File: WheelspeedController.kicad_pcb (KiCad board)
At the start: 2 copper layers, 63.5 x 35.3 mm, 70 parts, among them J1 DEUTSCH DT Inp, J2 DEUTSCH DT Data, J3 DEUTSCH DT Out, J4 Conn_01x02, J6 SWD, SW1 SW_SPDT, SW2 SW_SPDT, U1 LMR51420, U2 AMS1117-3.3, U3 STM32F105RCTx, U4 SN65HVD230, Y1 16MHz

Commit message: fixed borders
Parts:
- moved TP2 2.17 mm to (118.4, 102.4)
- moved TP4 2.05 mm to (61.0, 102.4)
- moved TP3 0.57 mm to (118.4, 73.2)
- moved TP1 0.25 mm to (61.0, 73.2)
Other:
- board size 63.5 x 35.3 mm -> 63.5 x 35.6 mm
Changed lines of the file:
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@@
   )
   (footprint "TestPoint:TestPoint_Plated_Hole_D3.0mm" (layer "F.Cu")
-    (at 61.976 100.584)
+    (at 60.96 102.362)
     (descr "Plated Hole as test Point, diameter 3.0mm")
     (tags "test point plated hole")
@@
   )
   (footprint "TestPoint:TestPoint_Plated_Hole_D3.0mm" (layer "F.Cu")
-    (at 60.96 73.406)
+    (at 60.96 73.152)
     (descr "Plated Hole as test Point, diameter 3.0mm")
     (tags "test point plated hole")
@@
   )
   (footprint "TestPoint:TestPoint_Plated_Hole_D3.0mm" (layer "F.Cu")
-    (at 116.332 101.6)
+    (at 118.364 102.362)
     (descr "Plated Hole as test Point, diameter 3.0mm")
     (tags "test point plated hole")
@@
   )
   (footprint "TestPoint:TestPoint_Plated_Hole_D3.0mm" (layer "F.Cu")
-    (at 117.856 73.406)
+    (at 118.364 73.152)
     (descr "Plated Hole as test Point, diameter 3.0mm")
     (tags "test point plated hole")
@@
     )
   )
-  (gr_rect (start 57.917 70.133) (end 121.417 105.439) (layer "Edge.Cuts") (width 0.1) (fill none))
+  (gr_rect (start 57.917 69.879) (end 121.417 105.439) (layer "Edge.Cuts") (width 0.1) (fill none))
   (segment (start 99.581 87.127) (end 100.579 87.127) (width 0.25) (layer "F.Cu") (net 1))
   (segment (start 90.113 91.243) (end 90.932 90.424) (width 0.25) (layer "F.Cu") (net 1))

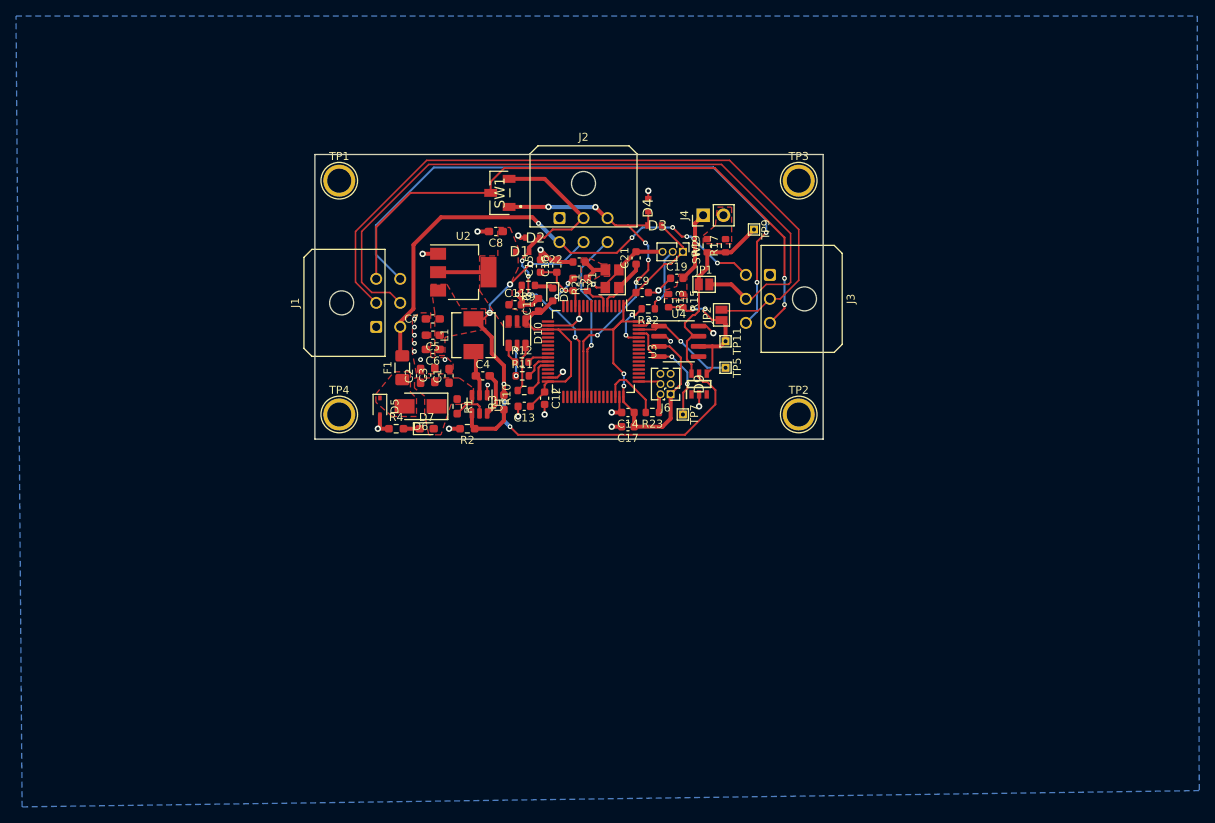
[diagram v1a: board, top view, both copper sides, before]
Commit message: Updated to 4 layers. Bit late
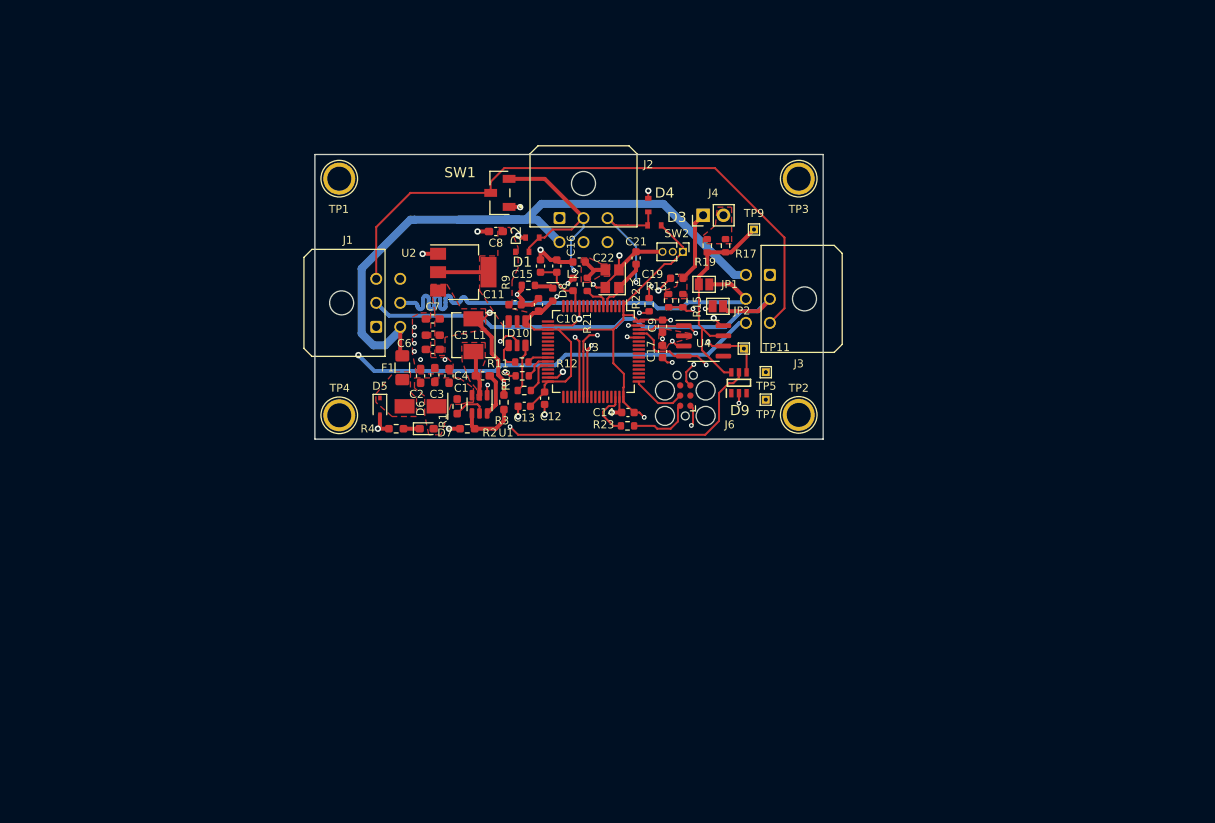
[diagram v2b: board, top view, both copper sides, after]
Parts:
- J6: footprint Connector_PinHeader_1.27mm:PinHeader_2x03_P1.27mm_Vertical -> Connector:Tag-Connect_TC2030-IDC-FP_2x03_P1.27mm_Vertical
- moved TP7 10.5 mm to (114.2, 100.5)
- moved C17 10.3 mm to (101.3, 94.5), turned to 90 degrees
- moved TP5 5.06 mm to (114.2, 97.1)
- moved D9 4.98 mm to (110.9, 98.4)
- moved C9 4.92 mm to (101.3, 91.3), turned to -90 degrees
- moved R23 3.52 mm to (97.0, 103.8)
- moved U4 3.10 mm to (106.5, 93.2)
- moved TP11 2.46 mm to (111.5, 94.1)
- moved J6 1.84 mm to (104.2, 100.0), turned to 90 degrees
- moved JP2 1.16 mm to (108.3, 88.8), turned to 0 degrees
- moved R22 0.52 mm to (99.7, 88.6), turned to -90 degrees
- moved TP1 0.25 mm to (61.0, 72.9)
- moved TP3 0.25 mm to (118.4, 72.9)
- moved TP4 0.10 mm to (61.0, 102.5)
- moved TP2 0.05 mm to (118.4, 102.4)
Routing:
- net /CAN+: track 90.7 -> 57.9 mm
- net /CAN-: track 90.3 -> 59.6 mm
- net +24V: track 63.2 -> 89.3 mm, vias 5 -> 0
- net /SHIELD: track 76.3 -> 64.9 mm, vias 2 -> 1
- net /MCU/CAN1_TX: track 13.2 -> 18.9 mm
- net Net-(J6-Pad2): track 2.37 -> 8.07 mm
- net Net-(D10-Pad5): track 3.30 -> 8.68 mm
- net /MCU/CAN1_RX: track 14.6 -> 19.9 mm, vias 2 -> 1
- net /MCU/SWCLK: track 2.84 -> 6.85 mm
- net +3V3: track 91.1 -> 94.9 mm, vias 4 -> 7
- net /WheelIn2: track 42.3 -> 44.5 mm, vias 4 -> 2
- net /MCU/SWDIO: track 8.21 -> 6.12 mm
- net +5V: track 67.7 -> 69.8 mm, vias 5 -> 3
- net Net-(D9-Pad6): track 25.9 -> 27.8 mm
- net /MCU/BOOT0: track 6.11 -> 7.56 mm
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- added copper zone on F.Cu, net /VRM/BUCK/SW
- added copper zone on In2.Cu, net GND
- removed copper zone on B.Cu, net GND
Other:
- copper layers 2 -> 4

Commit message: Aligned connectors
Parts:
- moved J2 1.71 mm to (87.2, 76.7)
- moved SW1 1.52 mm to (79.5, 74.7)
- moved TP1 1.05 mm to (62.0, 72.6)
- moved TP4 1.02 mm to (62.0, 102.5)
- moved D2 0.92 mm to (84.3, 79.8)
- moved C8 0.76 mm to (79.8, 79.5)
- moved J1 0.76 mm to (65.6, 90.7)
- moved J3 0.25 mm to (114.8, 84.7)
- moved TP3 0.25 mm to (118.4, 72.6)
- moved TP2 0.20 mm to (118.4, 102.6)
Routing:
- net +24V: track 89.3 -> 82.2 mm, vias 0 -> 4
- net /WheelIn1: track 47.2 -> 49.9 mm, vias 3 -> 4
- net /PassThru: track 76.4 -> 78.8 mm
- net /WheelIn2: track 44.5 -> 45.5 mm, vias 2 -> 3
- net +5V: track 69.8 -> 68.9 mm
- net /SHIELD: track 64.9 -> 65.7 mm
- net +3V3: track 94.9 -> 95.6 mm
- net /Extra1: track 21.5 -> 22.0 mm
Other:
- board size 63.5 x 35.6 mm -> 62.5 x 35.6 mm

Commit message: gerbers
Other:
- outline, holes or cut-outs redrawn
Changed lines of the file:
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@@
       (layerselection 0x00010fc_ffffffff)
       (disableapertmacros false)
-      (usegerberextensions false)
+      (usegerberextensions true)
       (usegerberattributes true)
       (usegerberadvancedattributes true)
@@
       (plotinvisibletext false)
       (sketchpadsonfab false)
-      (subtractmaskfromsilk false)
+      (subtractmaskfromsilk true)
       (outputformat 1)
       (mirror false)
-      (drillshape 1)
+      (drillshape 0)
       (scaleselection 1)
-      (outputdirectory "")
+      (outputdirectory "Gerbers/")
     )
   )
@@
     (fp_line (start -0.75 0.99) (end 0 0) (layer "F.Fab") (width 0.1))
     (pad "" np_thru_hole circle locked (at 3 -4.32) (size 3 3) (drill 3) (layers *.Cu *.Mask))
-    (pad "1" thru_hole roundrect locked (at 0 0) (size 1.5 1.5) (drill 1.02) (layers *.Cu *.Mask) (roundrect_rratio 0.166667)
+    (pad "1" thru_hole roundrect locked (at 0 0) (size 1.5 1.5) (drill 1.02) (layers *.Cu *.Mask) (roundrect_rratio 0.1666673333)
       (net 1 "GND") (pinfunction "Pin_1") (pintype "passive"))
     (pad "2" thru_hole circle locked (at 3 0) (size 1.5 1.5) (drill 1.02) (layers *.Cu *.Mask)
@@
     (fp_line (start 1.6 0.8) (end -1.6 0.8) (layer "F.Fab") (width 0.1))
     (fp_line (start 1.6 -0.8) (end 1.6 0.8) (layer "F.Fab") (width 0.1))
-    (pad "1" smd roundrect locked (at -1.4875 0 90) (size 1.425 1.75) (layers "F.Cu" "F.Paste" "F.Mask") (roundrect_rratio 0.175439)
+    (pad "1" smd roundrect locked (at -1.4875 0 90) (size 1.425 1.75) (layers "F.Cu" "F.Paste" "F.Mask") (roundrect_rratio 0.1754392982)
       (net 17 "/VRM/DIODE") (pintype "passive"))
-    (pad "2" smd roundrect locked (at 1.4875 0 90) (size 1.425 1.75) (layers "F.Cu" "F.Paste" "F.Mask") (roundrect_rratio 0.175439)
+    (pad "2" smd roundrect locked (at 1.4875 0 90) (size 1.425 1.75) (layers "F.Cu" "F.Paste" "F.Mask") (roundrect_rratio 0.1754392982)
       (net 76 "+24V") (pintype "passive"))
     (model "${KISYS3DMOD}/Fuse.3dshapes/Fuse_1206_3216Metric.wrl"
@@
     (fp_line (start 9.575 -7.92) (end 9.575 0.99) (layer "F.Fab") (width 0.1))
     (pad "" np_thru_hole circle locked (at 3 -4.32 90) (size 3 3) (drill 3) (layers *.Cu *.Mask))
-    (pad "1" thru_hole roundrect locked (at 0 0 90) (size 1.5 1.5) (drill 1.02) (layers *.Cu *.Mask) (roundrect_rratio 0.166667)
+    (pad "1" thru_hole roundrect locked (at 0 0 90) (size 1.5 1.5) (drill 1.02) (layers *.Cu *.Mask) (roundrect_rratio 0.1666673333)
       (net 1 "GND") (pinfunction "Pin_1") (pintype "passive"))
     (pad "2" thru_hole circle locked (at 3 0 90) (size 1.5 1.5) (drill 1.02) (layers *.Cu *.Mask)
@@
     (fp_line (start 9.575 0.99) (end -3.575 0.99) (layer "F.Fab") (width 0.1))
     (pad "" np_thru_hole circle locked (at 3 -4.32 270) (size 3 3) (drill 3) (layers *.Cu *.Mask))
-    (pad "1" thru_hole roundrect locked (at 0 0 270) (size 1.5 1.5) (drill 1.02) (layers *.Cu *.Mask) (roundrect_rratio 0.166667)
+    (pad "1" thru_hole roundrect locked (at 0 0 270) (size 1.5 1.5) (drill 1.02) (layers *.Cu *.Mask) (roundrect_rratio 0.1666673333)
       (net 1 "GND") (pinfunction "Pin_1") (pintype "passive"))
     (pad "2" thru_hole circle locked (at 3 0 270) (size 1.5 1.5) (drill 1.02) (layers *.Cu *.Mask)
@@
       (net 23 "unconnected-(J6-Pad6)") (pinfunction "Pin_6") (pintype "passive+no_connect"))
   )
-  (gr_rect (start 58.933 69.879) (end 121.417 105.439) (layer "Edge.Cuts") (width 0.1) (fill none))
+  (gr_arc (start 121.412 104.394) (mid 121.11442 105.11242) (end 120.396 105.41) (layer "Edge.Cuts") (width 0.1))
+  (gr_line (start 59.944 69.85) (end 120.65 69.85) (layer "Edge.Cuts") (width 0.1))
+  (gr_line (start 121.412 70.612) (end 121.412 104.394) (layer "Edge.Cuts") (width 0.1))
+  (gr_arc (start 120.65 69.85) (mid 121.188815 70.073185) (end 121.412 70.612) (layer "Edge.Cuts") (width 0.1))
+  (gr_arc (start 58.928 70.866) (mid 59.22558 70.14758) (end 59.944 69.85) (layer "Edge.Cuts") (width 0.1))
+  (gr_line (start 120.396 105.41) (end 59.944 105.439) (layer "Edge.Cuts") (width 0.1))
+  (gr_line (start 58.899 104.394) (end 58.928 70.866) (layer "Edge.Cuts") (width 0.1))
+  (gr_arc (start 59.944 105.439) (mid 59.205073 105.132927) (end 58.899 104.394) (layer "Edge.Cuts") (width 0.1))
   (segment (start 90.113 91.243) (end 90.932 90.424) (width 0.25) (layer "F.Cu") (net 1))
   (segment (start 78.8935 79.502) (end 77.47 79.502) (width 0.5) (layer "F.Cu") (net 1))
